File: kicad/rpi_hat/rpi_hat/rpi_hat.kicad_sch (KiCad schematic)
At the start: 11 parts, among them J1 GPIO, J2 FrontButtons, J3 DisplaySPI, J4 BatteryLevel, J5 PowerButton, J6 PowerWakeup

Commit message: WIP
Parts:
- removed J1: GPIO, Connector_PinSocket_2.54mm:PinSocket_2x20_P2.54mm_Vertical, symbol Connector_Generic:Conn_02x20_Odd_Even
- removed J2: FrontButtons, Connector_JST:JST_XH_S8B-XH-A_1x08_P2.50mm_Horizontal, symbol Connector:Conn_01x08_Pin
- removed J3: DisplaySPI, Connector_PinHeader_2.00mm:PinHeader_1x08_P2.00mm_Vertical, symbol Connector:Conn_01x08_Pin
- removed J4: BatteryLevel, Connector_JST:JST_XH_S4B-XH-A_1x04_P2.50mm_Horizontal, symbol Connector:Conn_01x04_Pin
- removed J5: PowerButton, Connector_JST:JST_XH_S2B-XH-A_1x02_P2.50mm_Horizontal, symbol Connector:Conn_01x02_Pin
- removed J6: PowerWakeup, Connector_JST:JST_XH_S2B-XH-A_1x02_P2.50mm_Horizontal, symbol Connector:Conn_01x02_Pin
- removed R3: 33k, Resistor_THT:R_Axial_DIN0207_L6.3mm_D2.5mm_P10.16mm_Horizontal, symbol Device:R
- added J1: FrontButtons, Connector_JST:JST_XH_S8B-XH-A_1x08_P2.50mm_Horizontal, symbol Connector:Conn_01x08_Pin
- added J2: PowerButton, Connector_JST:JST_XH_S2B-XH-A_1x02_P2.50mm_Horizontal, symbol Connector:Conn_01x02_Pin
- added J3: PowerWakeup, Connector_JST:JST_XH_S2B-XH-A_1x02_P2.50mm_Horizontal, symbol Connector:Conn_01x02_Pin
- added J4: DisplaySPI, Connector_JST:JST_PH_S8B-PH-K_1x08_P2.00mm_Horizontal, symbol Connector:Conn_01x08_Pin
- added J5: BatteryLevel, Connector_JST:JST_XH_S4B-XH-A_1x04_P2.50mm_Horizontal, symbol Connector:Conn_01x04_Pin
- added J6: GPIO, Connector_PinSocket_2.54mm:PinSocket_2x20_P2.54mm_Vertical, symbol Connector_Generic:Conn_02x20_Odd_Even
- added R1: 47k, Resistor_THT:R_Axial_DIN0207_L6.3mm_D2.5mm_P10.16mm_Horizontal, symbol Device:R
- R2: value 47k -> 33k
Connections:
- net SPI_GND is gone; now on net GND: C1.2, C2.2, C3.2
- net +3V3: now also J1.1 (Pin_1), J2.1 (Pin_1), J6.1 (Pin_1), J6.17 (Pin_17)
- net +5V: now also J4.1 (Pin_1), J6.2 (Pin_2), J6.4 (Pin_4)
- net BatterINP16: now also R2.2, J6.31 (Pin_31), R1.1; no longer R2.1
- net BatteryPwr: now also J5.1 (Pin_1), R1.2; no longer R2.2
- net Btn1: now also J1.8 (Pin_8), J6.16 (Pin_16)
- net Btn2: now also J1.7 (Pin_7), J6.13 (Pin_13)
- net Btn3: now also J1.6 (Pin_6), J6.12 (Pin_12)
- net Btn4: now also J1.5 (Pin_5), J6.11 (Pin_11)
- net Btn5: now also J1.4 (Pin_4), J6.10 (Pin_10)
- net Btn6: now also J1.3 (Pin_3), J6.7 (Pin_7)
- net BtnPower: now also J2.2 (Pin_2), J3.2 (Pin_2), J6.18 (Pin_18)
- net GND: now also R2.1, J4.2 (Pin_2), J5.4 (Pin_4), J6.14 (Pin_14), J6.20 (Pin_20), J6.25 (Pin_25), J6.30 (Pin_30), J6.33 (Pin_33), J6.34 (Pin_34), J6.39 (Pin_39), J6.6 (Pin_6), J6.9 (Pin_9)
- net GPIO10/SPI0.MOSI: now also J4.4 (Pin_4), J6.19 (Pin_19)
- net GPIO11/SPI0.SCLK: now also J4.5 (Pin_5), J6.23 (Pin_23)
- net GPIO12/PWM0: now also J6.32 (Pin_32)
- net GPIO14/TXD0: now also J6.8 (Pin_8)
- net GPIO16: now also J6.36 (Pin_36)
- net GPIO19/PCM.FS: now also J6.35 (Pin_35)
- net GPIO20/PCM.DIN: now also J6.38 (Pin_38)
- net GPIO21/PCM.DOUT: now also J6.40 (Pin_40)
- net GPIO22: now also J6.15 (Pin_15)
- net GPIO25: now also J6.22 (Pin_22)
- net GPIO26: now also J6.37 (Pin_37)
- net GPIO2/SDA1: now also J6.3 (Pin_3)
- net GPIO3/SCL1: now also J6.5 (Pin_5)
- net GPIO5: now also J4.7 (Pin_7), J6.29 (Pin_29)
- net GPIO7/SPI0.CE1: now also J4.8 (Pin_8), J6.26 (Pin_26)
- net GPIO8/SPI0.CE0: now also J4.6 (Pin_6), J6.24 (Pin_24)
- net GPIO9/SPI0.MISO: now also J4.3 (Pin_3), J6.21 (Pin_21)
- net ID_SCL: now also J6.28 (Pin_28)
- net ID_SDA: now also J6.27 (Pin_27)
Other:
- note removed: "Additional pin functions: https://pinout.xyz/"

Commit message: add power switch to it8951
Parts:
- removed C1: 0.1uF, Capacitor_THT:C_Disc_D10.0mm_W2.5mm_P5.00mm, symbol Device:C
- removed C2: 10uF, Capacitor_THT:C_Disc_D10.0mm_W2.5mm_P5.00mm, symbol Device:C
- removed C3: 220nF, Capacitor_THT:C_Radial_D8.0mm_H7.0mm_P3.50mm, symbol Device:C
- added Q1: AO3401A, Package_TO_SOT_SMD:SOT-23, symbol Transistor_FET:AO3401A
- added Q2: PN2222A, Package_TO_SOT_THT:TO-92_Inline, symbol Transistor_BJT:PN2222A
- added R3, R4: 10k, Resistor_THT:R_Axial_DIN0207_L6.3mm_D2.5mm_P10.16mm_Horizontal, symbol Device:R
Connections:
- net +5V: now also Q1.2 (S), R3.2; no longer J4.1 (Pin_1)
- net GND: now also Q2.1 (E)
- net GPIO12/PWM0: now also R4.2
- new net: Q2.2 (B), R4.1
- new net: Q1.1 (G), Q2.3 (C), R3.1
- new net SPI_PWR: J4.1 (Pin_1), Q1.3 (D)
- no-connect marks 17 -> 16

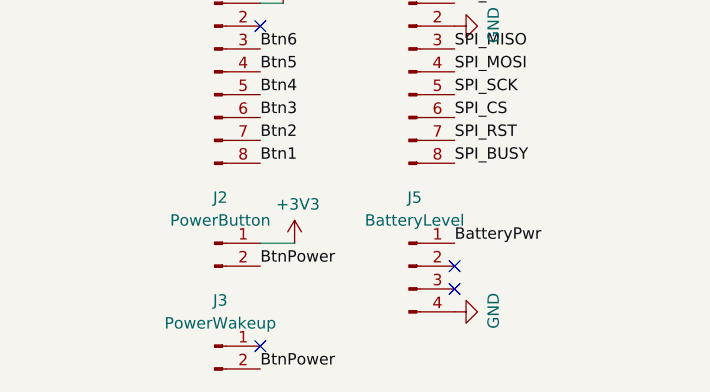
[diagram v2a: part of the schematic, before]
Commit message: fix bug in power on button routing in hat
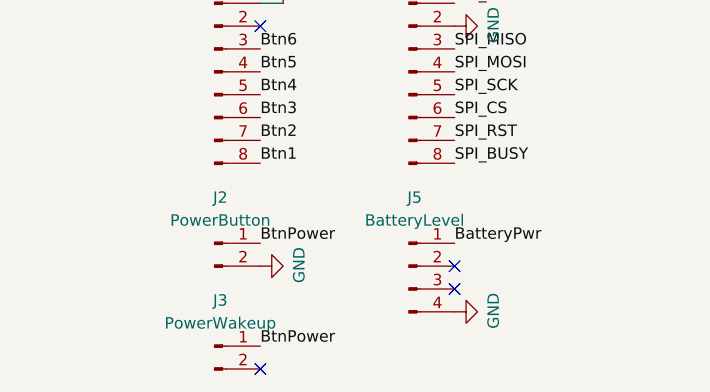
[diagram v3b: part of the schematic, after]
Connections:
- net +3V3: no longer J2.1 (Pin_1)
- net BtnPower: now also J2.1 (Pin_1), J3.1 (Pin_1); no longer J2.2 (Pin_2), J3.2 (Pin_2)
- net GND: now also J2.2 (Pin_2)
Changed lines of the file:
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@@
-	)
-	(no_connect
-		(at 45.72 146.05)
 	)
 	(no_connect
@@
 	)
 	(no_connect
+		(at 45.72 148.59)
+	)
+	(no_connect
 		(at 45.72 110.49)
 	)
@@
 	(wire
 		(pts
-			(xy 45.72 134.62) (xy 49.53 134.62)
-		)
-		(stroke
-			(width 0)
-			(type default)
-		)
-	)
-	(wire
-		(pts
 			(xy 67.31 53.34) (xy 67.31 73.66)
 		)
@@
 		)
 	)
-	(label "BtnPower"
-		(at 45.72 148.59 0)
-		(effects
-			(font
-				(size 1.27 1.27)
-			)
-			(justify left bottom)
-		)
-	)
 	(label "SPI_PWR"
 		(at 67.31 107.95 0)
@@
 		)
 	)
+	(label "BtnPower"
+		(at 45.72 134.62 0)
+		(effects
+			(font
+				(size 1.27 1.27)
+			)
+			(justify left bottom)
+		)
+	)
 	(label "GPIO24"
 		(at 109.22 63.5 180)
@@
 		)
 	)
+	(label "BtnPower"
+		(at 45.72 146.05 0)
+		(effects
+			(font
+				(size 1.27 1.27)
+			)
+			(justify left bottom)
+		)
+	)
 	(label "GPIO26"
 		(at 40.64 88.9 0)
@@
 		)
 	)
-	(label "BtnPower"
-		(at 45.72 137.16 0)
-		(effects
-			(font
-				(size 1.27 1.27)
-			)
-			(justify left bottom)
-		)
-	)
 	(label "Btn3"
 		(at 45.72 120.65 0)
@@
 			)
 			(justify right bottom)
+		)
+	)
+	(symbol
+		(lib_id "power:GND")
+		(at 45.72 137.16 90)
+		(unit 1)
+		(body_style 1)
+		(exclude_from_sim no)
+		(in_bom yes)
+		(on_board yes)
+		(in_pos_files yes)
+		(dnp no)
+		(property "Reference" "#PWR013"
+			(at 52.07 137.16 0)
+			(hide yes)
+			(show_name no)
+			(do_not_autoplace no)
+			(effects
+				(font
+					(size 1.27 1.27)
+				)
+			)
+		)
+		(property "Value" "GND"
+			(at 50.0444 137.0457 0)
+			(show_name no)
+			(do_not_autoplace no)
+			(effects
+				(font
+					(size 1.27 1.27)
+				)
+			)
+		)
+		(property "Footprint" ""
+			(at 45.72 137.16 0)
+			(show_name no)
+			(do_not_autoplace no)
+			(effects
+				(font
+					(size 1.27 1.27)
+				)
+			)
+		)
+		(property "Datasheet" ""
+			(at 45.72 137.16 0)
+			(show_name no)
+			(do_not_autoplace no)
+			(effects
+				(font
+					(size 1.27 1.27)
+				)
+			)
+		)
+		(property "Description" "Power symbol creates a global label with name \"GND\" , ground"
+			(at 45.72 137.16 0)
+			(hide yes)
+			(show_name no)
+			(do_not_autoplace no)
+			(effects
+				(font
+					(size 1.27 1.27)
+				)
+			)
+		)
+		(pin "1"
+		)
+		(instances
+			(project "rpi_hat"
+				(path "/e63e39d7-6ac0-4ffd-8aa3-1841a4541b55"
+					(reference "#PWR013")
+					(unit 1)
+				)
+			)
 		)
 	)
@@
 					(unit 1)
 				)
-			)
-		)
-	)
-	(symbol
-		(lib_id "power:+3.3V")
-		(at 49.53 134.62 0)
-		(unit 1)
-		(body_style 1)
-		(exclude_from_sim no)
-		(in_bom yes)
-		(on_board yes)
-		(in_pos_files yes)
-		(dnp no)
-		(property "Reference" "#PWR02"
-			(at 49.53 138.43 0)
-			(hide yes)
-			(show_name no)
-			(do_not_autoplace no)
-			(effects
-				(font
-					(size 1.27 1.27)
-				)
-			)
-		)
-		(property "Value" "+3V3"
-			(at 49.8983 130.2956 0)
-			(show_name no)
-			(do_not_autoplace no)
-			(effects
-				(font
-					(size 1.27 1.27)
-				)
-			)
-		)
-		(property "Footprint" ""
-			(at 49.53 134.62 0)
-			(show_name no)
-			(do_not_autoplace no)
-			(effects
-				(font
-					(size 1.27 1.27)
-				)
-			)
-		)
-		(property "Datasheet" ""
-			(at 49.53 134.62 0)
-			(show_name no)
-			(do_not_autoplace no)
-			(effects
-				(font
-					(size 1.27 1.27)
-				)
-			)
-		)
-		(property "Description" "Power symbol creates a global label with name \"+3.3V\""
-			(at 49.53 134.62 0)
-			(hide yes)
-			(show_name no)
-			(do_not_autoplace no)
-			(effects
-				(font
-					(size 1.27 1.27)
-				)
-			)
-		)
-		(pin "1"
-		)
-		(instances
-			(project "rpi_hat"
-				(path "/e63e39d7-6ac0-4ffd-8aa3-1841a4541b55"
-					(reference "#PWR02")
-					(unit 1)
-				)

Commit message: wip
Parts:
- added R5: 10k, Resistor_THT:R_Axial_DIN0207_L6.3mm_D2.5mm_P10.16mm_Horizontal, symbol Device:R
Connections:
- net BatteryPwr: now also J5.3 (Pin_3); no longer J5.1 (Pin_1)
- net BtnPower: now also R5.2; no longer J3.1 (Pin_1)
- new net: J3.1 (Pin_1), R5.1
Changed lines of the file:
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@@
-	)
-	(no_connect
-		(at 67.31 139.7)
 	)
 	(no_connect
@@
 	)
 	(no_connect
+		(at 67.31 133.35)
+	)
+	(no_connect
 		(at 109.22 50.8)
 	)
@@
 	)
 	(no_connect
-		(at 67.31 137.16)
-	)
-	(no_connect
 		(at 45.72 148.59)
 	)
@@
 		(at 109.22 68.58)
 	)
+	(no_connect
+		(at 67.31 135.89)
+	)
 	(wire
 		(pts
@@
 	(wire
 		(pts
+			(xy 45.72 146.05) (xy 49.53 146.05)
+		)
+		(stroke
+			(width 0)
+			(type default)
+		)
+	)
+	(wire
+		(pts
 			(xy 172.72 41.91) (xy 161.29 41.91)
 		)
@@
 		(pts
 			(xy 187.96 60.96) (xy 186.69 60.96)
+		)
+		(stroke
+			(width 0)
+			(type default)
+		)
+	)
+	(wire
+		(pts
+			(xy 57.15 146.05) (xy 60.96 146.05)
 		)
 		(stroke
@@
 	)
 	(label "BatteryPwr"
+		(at 67.31 138.43 0)
+		(effects
+			(font
+				(size 1.27 1.27)
+			)
+			(justify left bottom)
+		)
+	)
+	(label "BatteryPwr"
 		(at 167.64 109.22 180)
 		(effects
@@
 		)
 	)
-	(label "BatteryPwr"
-		(at 67.31 134.62 0)
-		(effects
-			(font
-				(size 1.27 1.27)
-			)
-			(justify left bottom)
-		)
-	)
 	(label "GPIO14{slash}TXD0"
 		(at 109.22 50.8 180)
@@
 		)
 	)
-	(label "BtnPower"
-		(at 45.72 146.05 0)
-		(effects
-			(font
-				(size 1.27 1.27)
-			)
-			(justify left bottom)
-		)
-	)
 	(label "GPIO26"
 		(at 40.64 88.9 0)
@@
 			)
 			(justify right bottom)
+		)
+	)
+	(label "BtnPower"
+		(at 60.96 146.05 0)
+		(effects
+			(font
+				(size 1.27 1.27)
+			)
+			(justify left bottom)
 		)
 	)
@@
 	)
 	(symbol
+		(lib_id "Device:R")
+		(at 53.34 146.05 90)
+		(unit 1)
+		(body_style 1)
+		(exclude_from_sim no)
+		(in_bom yes)
+		(on_board yes)
+		(in_pos_files yes)
+		(dnp no)
+		(property "Reference" "R5"
+			(at 53.34 146.05 90)
+			(show_name no)
+			(do_not_autoplace no)
+			(effects
+				(font
+					(size 1.27 1.27)
+				)
+			)
+		)
+		(property "Value" "10k"
+			(at 53.34 148.59 90)
+			(show_name no)
+			(do_not_autoplace no)
+			(effects
+				(font
+					(size 1.27 1.27)
+				)
+			)
+		)
+		(property "Footprint" "Resistor_THT:R_Axial_DIN0207_L6.3mm_D2.5mm_P10.16mm_Horizontal"
+			(at 53.34 147.828 90)
+			(hide yes)
+			(show_name no)
+			(do_not_autoplace no)
+			(effects
+				(font
+					(size 1.27 1.27)
+				)
+			)
+		)
+		(property "Datasheet" ""
+			(at 53.34 146.05 0)
+			(hide yes)
+			(show_name no)
+			(do_not_autoplace no)
+			(effects
+				(font
+					(size 1.27 1.27)
+				)
+			)
+		)
+		(property "Description" "Resistor"
+			(at 53.34 146.05 0)
+			(hide yes)
+			(show_name no)
+			(do_not_autoplace no)
+			(effects
+				(font
+					(size 1.27 1.27)
+				)
+			)
+		)
+		(pin "2"
+		)
+		(pin "1"
+		)
+		(instances
+			(project "rpi_hat"
+				(path "/e63e39d7-6ac0-4ffd-8aa3-1841a4541b55"
+					(reference "R5")
+					(unit 1)
+				)
+			)
+		)
+	)
+	(symbol
 		(lib_id "Transistor_FET:AO3401A")
 		(at 163.83 49.53 180)
@@
 	)
 	(symbol
-		(lib_id "power:GND")
-		(at 67.31 142.24 90)
-		(unit 1)
-		(body_style 1)
-		(exclude_from_sim no)
-		(in_bom yes)
-		(on_board yes)
-		(in_pos_files yes)
-		(dnp no)
-		(property "Reference" "#PWR09"
-			(at 73.66 142.24 0)
-			(hide yes)
-			(show_name no)
-			(do_not_autoplace no)
-			(effects
-				(font
-					(size 1.27 1.27)
-				)
-			)
-		)
-		(property "Value" "GND"
-			(at 71.6344 142.1257 0)
-			(show_name no)
-			(do_not_autoplace no)
-			(effects
-				(font
-					(size 1.27 1.27)
-				)
-			)
-		)
-		(property "Footprint" ""
-			(at 67.31 142.24 0)
-			(show_name no)
-			(do_not_autoplace no)
-			(effects
-				(font
-					(size 1.27 1.27)
-				)
-			)
-		)
-		(property "Datasheet" ""
-			(at 67.31 142.24 0)
-			(show_name no)
-			(do_not_autoplace no)
-			(effects
-				(font
-					(size 1.27 1.27)
-				)
-			)
-		)
-		(property "Description" "Power symbol creates a global label with name \"GND\" , ground"
-			(at 67.31 142.24 0)
-			(hide yes)
-			(show_name no)
-			(do_not_autoplace no)
-			(effects
-				(font
-					(size 1.27 1.27)
-				)
-			)
-		)
-		(pin "1"
-		)
-		(instances
-			(project "rpi_hat"
-				(path "/e63e39d7-6ac0-4ffd-8aa3-1841a4541b55"
-					(reference "#PWR09")
-					(unit 1)
-				)
-			)
-		)
-	)
-	(symbol
 		(lib_id "power:+5V")
 		(at 85.09 39.37 0)
@@
 	)
 	(symbol
+		(lib_id "power:GND")
+		(at 67.31 140.97 90)
+		(unit 1)
+		(body_style 1)
+		(exclude_from_sim no)
+		(in_bom yes)
+		(on_board yes)
+		(in_pos_files yes)
+		(dnp no)
+		(property "Reference" "#PWR09"
+			(at 73.66 140.97 0)
+			(hide yes)
+			(show_name no)
+			(do_not_autoplace no)
+			(effects
+				(font
+					(size 1.27 1.27)
+				)
+			)
+		)
+		(property "Value" "GND"
+			(at 71.6344 140.8557 0)
+			(show_name no)
+			(do_not_autoplace no)
+			(effects
+				(font
+					(size 1.27 1.27)
+				)
+			)
+		)
+		(property "Footprint" ""
+			(at 67.31 140.97 0)
+			(show_name no)
+			(do_not_autoplace no)
+			(effects
+				(font
+					(size 1.27 1.27)
+				)
+			)
+		)
+		(property "Datasheet" ""
+			(at 67.31 140.97 0)
+			(show_name no)
+			(do_not_autoplace no)
+			(effects
+				(font
+					(size 1.27 1.27)
+				)
+			)
+		)
+		(property "Description" "Power symbol creates a global label with name \"GND\" , ground"
+			(at 67.31 140.97 0)
+			(hide yes)
+			(show_name no)
+			(do_not_autoplace no)
+			(effects
+				(font
+					(size 1.27 1.27)
+				)
+			)
+		)
+		(pin "1"
+		)
+		(instances
+			(project "rpi_hat"
+				(path "/e63e39d7-6ac0-4ffd-8aa3-1841a4541b55"
+					(reference "#PWR09")
+					(unit 1)
+				)
+			)
+		)
+	)
+	(symbol
 		(lib_id "power:+3.3V")
 		(at 48.26 107.95 0)
@@
 	(symbol
 		(lib_id "Connector:Conn_01x04_Pin")
-		(at 62.23 137.16 0)
+		(at 62.23 135.89 0)
 		(unit 1)
 		(body_style 1)
@@
 		(fields_autoplaced yes)
 		(property "Reference" "J5"
-			(at 62.865 129.54 0)
+			(at 62.865 128.27 0)
 			(show_name no)
 			(do_not_autoplace no)
@@
 		)
 		(property "Value" "BatteryLevel"
-			(at 62.865 132.08 0)
+			(at 62.865 130.81 0)
 			(show_name no)
 			(do_not_autoplace no)
@@
 		)
 		(property "Footprint" "Connector_JST:JST_XH_S4B-XH-A_1x04_P2.50mm_Horizontal"
-			(at 62.23 137.16 0)
+			(at 62.23 135.89 0)
 			(hide yes)
 			(show_name no)
@@
 		)
 		(property "Datasheet" ""
-			(at 62.23 137.16 0)
+			(at 62.23 135.89 0)
 			(hide yes)
 			(show_name no)
@@
 		)
 		(property "Description" "Generic connector, single row, 01x04, script generated"
-			(at 62.23 137.16 0)
-			(hide yes)
-			(show_name no)
+			(at 62.23 135.89 0)
+			(hide yes)
+			(show_name no)

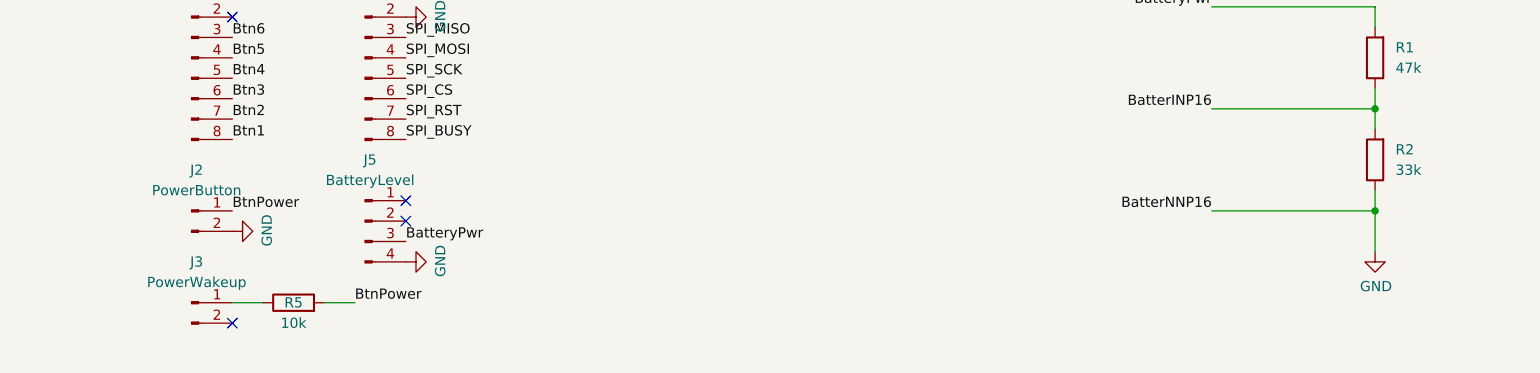
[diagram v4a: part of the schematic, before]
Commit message: Add support for battery (#10)
* add program to read voltage from adc and fix hat

* add battery support in lvgl
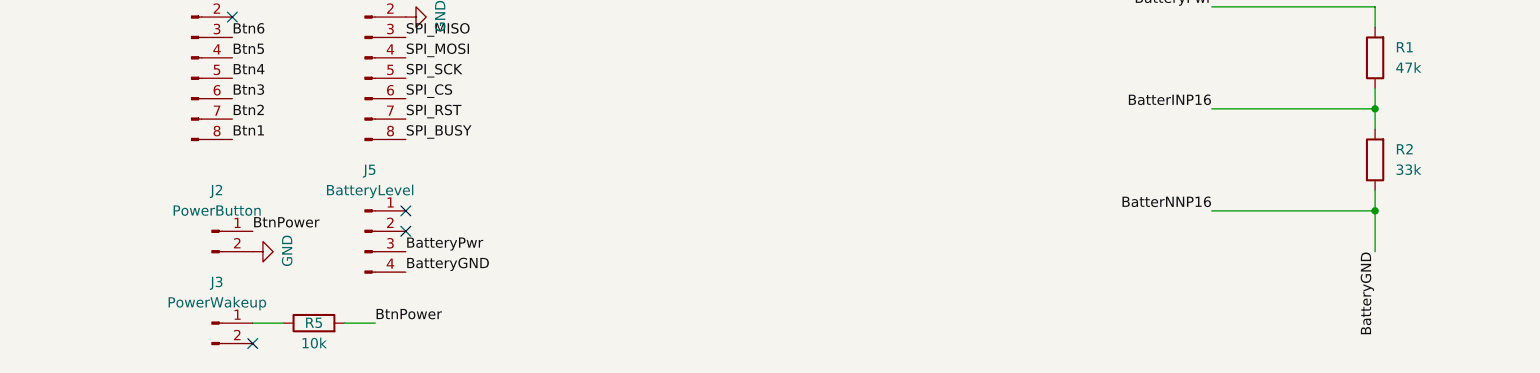
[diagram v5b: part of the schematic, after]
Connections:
- net GND: no longer J5.4 (Pin_4), J6.33 (Pin_33), R2.1
- new net BatterNNP16: J5.4 (Pin_4), J6.33 (Pin_33), R2.1
